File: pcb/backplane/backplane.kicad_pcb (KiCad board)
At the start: 2 copper layers, 12 parts

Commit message: footprints
added footprints
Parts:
- added JST1: B4B-XH-A, backplane:B4B-XH-A, F.Cu at (62.0, -44.0)
- added JST2: B4B-XH-A, backplane:B4B-XH-A, F.Cu at (44.9, -30.9)
- added JST3: B4B-XH-A, backplane:B4B-XH-A, F.Cu at (44.9, -25.0)
- added JST4: B4B-XH-A, backplane:B4B-XH-A, F.Cu at (62.0, -38.1)
- added Motor1Header1: PRPC006SAAN-RC, backplane:PRPC006SAAN-RC, F.Cu at (28.4, -43.9)
- added Motor1Header2: PRPC006SAAN-RC, backplane:PRPC006SAAN-RC, F.Cu at (28.4, -40.7)
- added Motor1Header3: PRPC006SAAN-RC, backplane:PRPC006SAAN-RC, F.Cu at (45.5, -43.9)
- added Motor2Header1: PRPC006SAAN-RC, backplane:PRPC006SAAN-RC, F.Cu at (28.4, -37.4)
- added Motor2Header2: PRPC006SAAN-RC, backplane:PRPC006SAAN-RC, F.Cu at (45.5, -40.7)
- added Motor2Header3: PRPC006SAAN-RC, backplane:PRPC006SAAN-RC, F.Cu at (28.4, -34.1)
- added Motor3Header1: PRPC006SAAN-RC, backplane:PRPC006SAAN-RC, F.Cu at (28.4, -30.8)
- added Motor3Header2: PRPC006SAAN-RC, backplane:PRPC006SAAN-RC, F.Cu at (28.4, -27.5)
- added Motor3Header3: PRPC006SAAN-RC, backplane:PRPC006SAAN-RC, F.Cu at (28.4, -24.2)
- added Motor4Header1: PRPC006SAAN-RC, backplane:PRPC006SAAN-RC, F.Cu at (28.4, -20.9)
- added Motor4Header2: PRPC006SAAN-RC, backplane:PRPC006SAAN-RC, F.Cu at (45.5, -37.4)
- added Motor4Header3: PRPC006SAAN-RC, backplane:PRPC006SAAN-RC, F.Cu at (45.5, -34.1)

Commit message: updated pcb
added footprints and schematic
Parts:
- removed Motor1Header1, Motor1Header2, Motor1Header3, Motor2Header1, Motor2Header2, Motor2Header3, Motor3Header1, Motor3Header2, Motor3Header3, Motor4Header1, Motor4Header2, Motor4Header3: PRPC006SAAN-RC, backplane:PRPC006SAAN-RC
- added JST5: B4B-XH-A, backplane:B4B-XH-A, F.Cu at (5.08, 87.7)
- added JST6: B4B-XH-A, backplane:B4B-XH-A, F.Cu at (5.08, 53.3)
- added JST7: B4B-XH-A, backplane:B4B-XH-A, F.Cu at (121.9, 53.3)
- added JST8: B4B-XH-A, backplane:B4B-XH-A, F.Cu at (121.9, 88.9)
- added U1: 74LVCH2T45DC,125, backplane:74LVCH2T45DC,125, F.Cu at (22.9, 30.5)
- added U2: 74LVCH2T45DC,125, backplane:74LVCH2T45DC,125, F.Cu at (22.9, 68.6)
- added U3: 74LVCH2T45DC,125, backplane:74LVCH2T45DC,125, F.Cu at (108.1, 30.7)
- added U4: 74LVCH2T45DC,125, backplane:74LVCH2T45DC,125, F.Cu at (106.7, 68.6)
- added barrelJack1: PJ-037A, backplane:PJ-037A, F.Cu at (64.8, 6.35)
- added barrelJack2: PJ-037A, backplane:PJ-037A, F.Cu at (77.5, 6.35)
- added barrelJack3: PJ-037A, backplane:PJ-037A, F.Cu at (53.3, 6.35)
- added encoderpins1: PREC002SAAN-RC, backplane:PREC002SAAN-RC, F.Cu at (34.3, 41.9)
- added encoderpins2: PREC002SAAN-RC, backplane:PREC002SAAN-RC, F.Cu at (33.0, 90.2)
- added encoderpins3: PREC002SAAN-RC, backplane:PREC002SAAN-RC, F.Cu at (94.0, 50.8)
- added encoderpins4: PREC002SAAN-RC, backplane:PREC002SAAN-RC, F.Cu at (94.0, 86.4)
- added encoderpins5: PREC002SAAN-RC, backplane:PREC002SAAN-RC, F.Cu at (34.3, 31.8)
- added encoderpins6: PREC002SAAN-RC, backplane:PREC002SAAN-RC, F.Cu at (33.0, 69.8)
- added encoderpins7: PREC002SAAN-RC, backplane:PREC002SAAN-RC, F.Cu at (94.0, 31.8)
- added encoderpins8: PREC002SAAN-RC, backplane:PREC002SAAN-RC, F.Cu at (94.0, 71.1)
- moved JST4 126.8 mm to (121.9, 73.7), turned to 90 degrees
- moved motor2Gnd1 120.1 mm to (119.4, 7.62), turned to 180 degrees
- moved motor3Gnd1 117.0 mm to (7.62, 119.4), turned to 0 degrees
- moved motor3Pwr1 117.0 mm to (7.62, 105.4), turned to 0 degrees
- moved motor2Pwr1 113.7 mm to (119.4, 21.6), turned to 180 degrees
- moved JST3 106.4 mm to (5.08, 73.7), turned to 270 degrees
- moved JST2 103.4 mm to (121.9, 38.1), turned to 90 degrees
- moved JST1 101.0 mm to (5.08, 39.4), turned to 270 degrees
- moved motor4Gnd1 86.7 mm to (119.4, 119.4), turned to 180 degrees
- moved motor4Pwr1 86.7 mm to (119.4, 105.4), turned to 180 degrees
- moved lipo2Gnd1 65.7 mm to (99.1, 119.4), turned to 180 degrees
- moved lipo1Gnd1 54.0 mm to (41.9, 119.4)
- moved lipo1Pwr1 54.0 mm to (27.9, 119.4)
- moved lipo2Pwr1 51.8 mm to (85.1, 119.4)
- moved motor1Pwr1 1.80 mm to (7.62, 7.62), turned to 0 degrees
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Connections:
- JST1 pad 1: Motor1EncoderPin1 -> +5V
- JST1 pad 2: Motor1EncoderPin2 -> GND
- JST1 pad 3: Motor1EncoderPin3 -> Motor1EncoderA
- JST1 pad 4: Motor1EncoderPin4 -> Motor1EncoderB
- JST2 pad 1: Motor2EncoderPin1 -> +5V
- JST2 pad 2: Motor2EncoderPin2 -> GND
- JST2 pad 3: Motor2EncoderPin3 -> Motor2EncoderA
- JST2 pad 4: Motor2EncoderPin4 -> Motor2EncoderB
- JST3 pad 1: Motor3EncoderPin1 -> +5V
- JST3 pad 2: Motor3EncoderPin2 -> GND
- JST3 pad 3: Motor3EncoderPin3 -> Motor3EncoderA
- JST3 pad 4: Motor3EncoderPin4 -> Motor3EncoderB
- JST4 pad 1: Motor4EncoderPin1 -> +5V
- JST4 pad 2: Motor4EncoderPin2 -> GND
- JST4 pad 3: Motor4EncoderPin3 -> Motor4EncoderA
- JST4 pad 4: Motor4EncoderPin4 -> Motor4EncoderB
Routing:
- net Motor2EncoderB: track 0.00 -> 2.62 mm
- net Motor2EncoderA: track 0.00 -> 2.57 mm
- net Motor1EncoderA: track 0.00 -> 2.46 mm
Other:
- board outline added: 127 x 127 mm
- net class Default: trace_width 0.25 -> 0.3; via_dia 0.8 -> 0.762; via_drill 0.4 -> 0.381
- rule pad_to_mask_clearance: 0.051 -> 0.0508
- rule trace_min: 0.2 -> 0.1524
- rule via_min_drill: 0.3 -> 0.254
- rule via_min_size: 0.4 -> 0.508

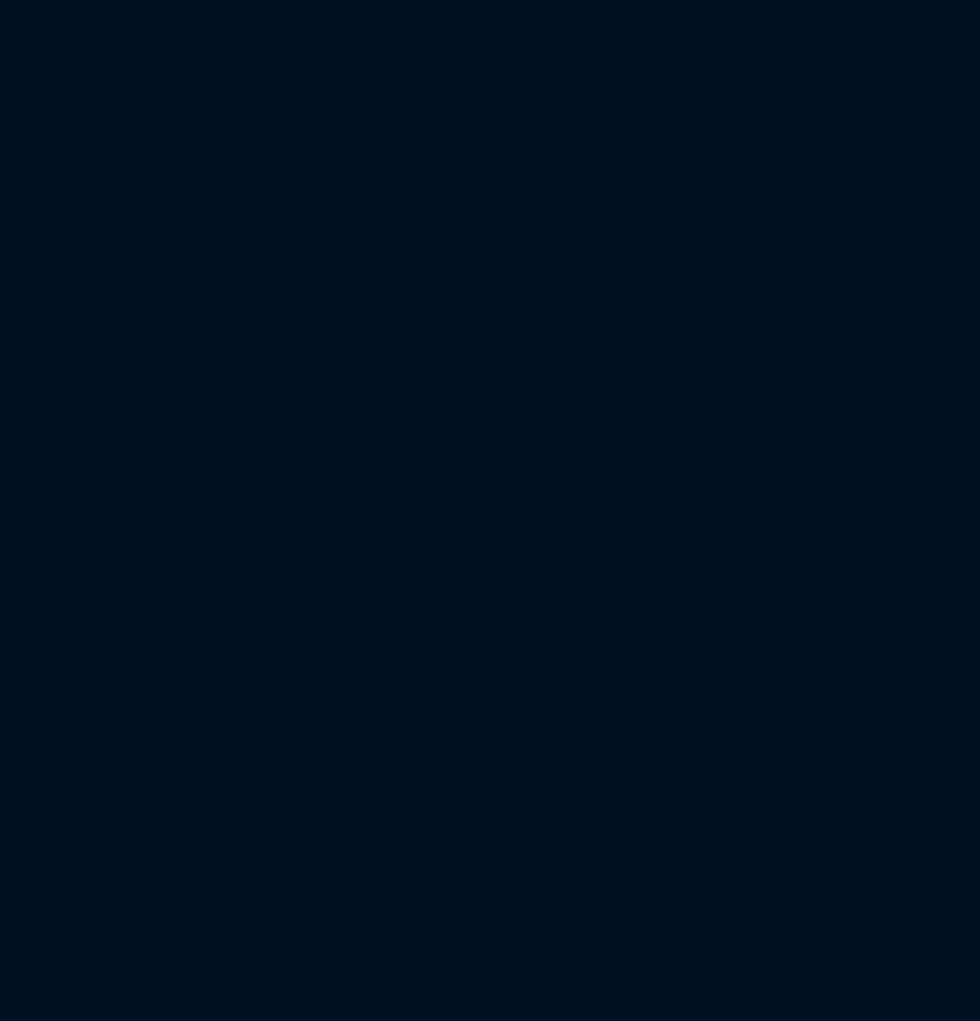
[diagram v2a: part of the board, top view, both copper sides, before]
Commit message: updated footprints
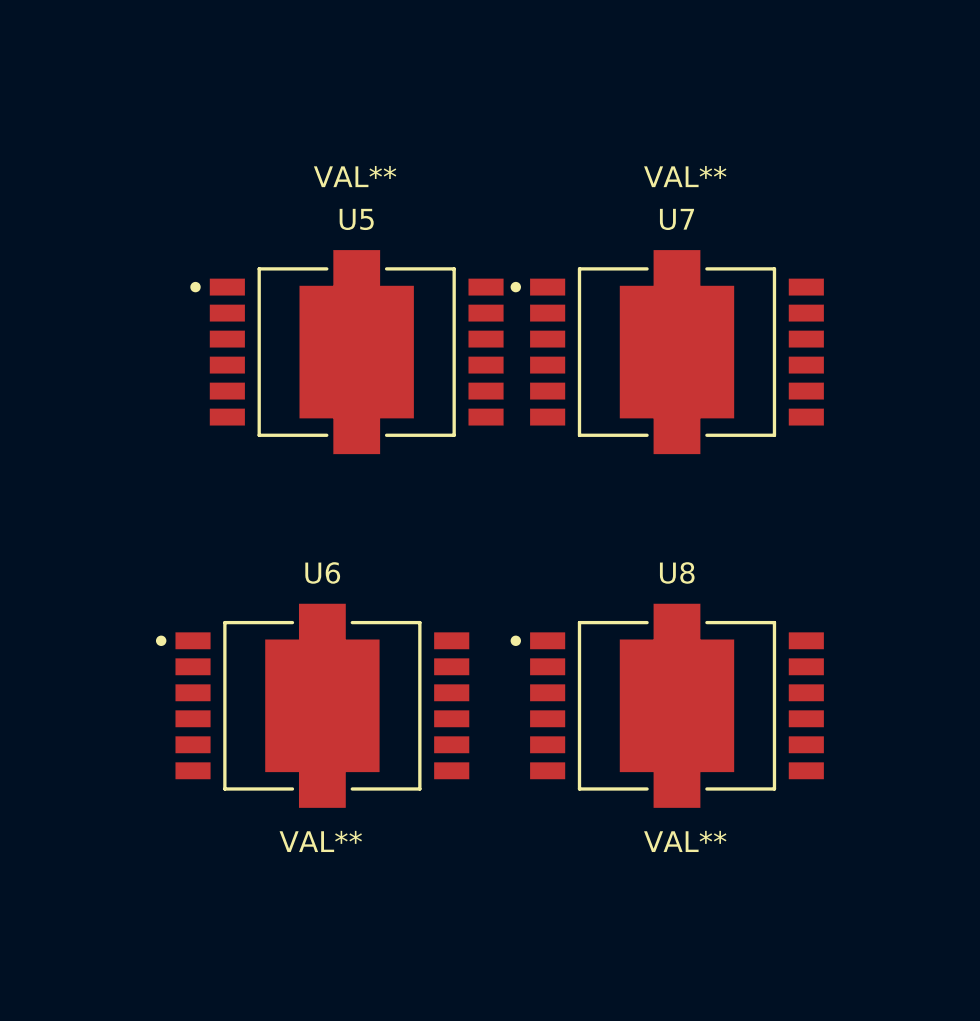
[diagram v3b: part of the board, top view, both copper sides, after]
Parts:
- added U5: VAL**, backplane:IFX9201SGAUMA1, F.Cu at (57.2, 46.1)
- added U6: VAL**, backplane:IFX9201SGAUMA1, F.Cu at (55.9, 59.7)
- added U7: VAL**, backplane:IFX9201SGAUMA1, F.Cu at (69.5, 46.1)
- added U8: VAL**, backplane:IFX9201SGAUMA1, F.Cu at (69.5, 59.7)

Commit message: updates
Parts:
- removed U2, U3, U4: 74LVCH2T45DC,125, backplane:74LVCH2T45DC,125
- removed lipo1Gnd1, lipo1Pwr1, lipo2Gnd1, lipo2Pwr1, motor1Gnd1, motor1Pwr1, motor2Gnd1, motor2Pwr1, motor3Gnd1, motor3Pwr1, motor4Gnd1, motor4Pwr1: CT3151V1-5, backplane:CT3151V1-5
- added LipoGnd1: 1336G1, backplane:1336G1, F.Cu at (54.6, 114.3)
- added levelShift1: 74LVCH2T45DC,125, backplane:74LVCH2T45DC,125, F.Cu at (20.3, 31.8)
- added levelShift2: 74LVCH2T45DC,125, backplane:74LVCH2T45DC,125, F.Cu at (102.9, 43.2)
- added levelShift3: 74LVCH2T45DC,125, backplane:74LVCH2T45DC,125, F.Cu at (16.5, 69.8)
- added levelShift4: 74LVCH2T45DC,125, backplane:74LVCH2T45DC,125, F.Cu at (108.0, 66.0)
- added lipoGnd1: 1336G1, backplane:1336G1, F.Cu at (85.1, 114.3)
- added lipoIn1: 1336G1, backplane:1336G1, F.Cu at (39.4, 114.3)
- added lipoIn2: 1336G1, backplane:1336G1, F.Cu at (69.8, 114.3)
- added motorGnd1: 1336G1, backplane:1336G1, F.Cu at (14.0, 22.9)
- added motorGnd2: 1336G1, backplane:1336G1, F.Cu at (113.0, 22.9)
- added motorGnd3: 1336G1, backplane:1336G1, F.Cu at (15.2, 119.4)
- added motorGnd4: 1336G1, backplane:1336G1, F.Cu at (111.8, 119.4)
- added motorPwm1: 1336G1, backplane:1336G1, F.Cu at (14.0, 7.62)
- added motorPwm2: 1336G1, backplane:1336G1, F.Cu at (113.0, 7.62)
- added motorPwm3: 1336G1, backplane:1336G1, F.Cu at (15.2, 104.1)
- added motorPwm4: 1336G1, backplane:1336G1, F.Cu at (111.8, 104.1)
- added rail12v1: AP6503SP-13, backplane:AP6503SP-13, F.Cu at (76.2, 27.9)
- added rail3v3: AP6503SP-13, backplane:AP6503SP-13, F.Cu at (64.8, 27.9)
- added rail5v1: AP6503SP-13, backplane:AP6503SP-13, F.Cu at (54.6, 27.9)
- U1: value 74LVCH2T45DC,125 -> PCA9685PW; footprint backplane:74LVCH2T45DC,125 -> Package_SO:TSSOP-28_4.4x9.7mm_P0.65mm
- U5, U6, U7, U8: value VAL** -> IFX9201SGAUMA1
- moved U7 71.4 mm to (31.8, 106.7)
- moved U6 63.8 mm to (99.1, 12.7)
- moved U8 56.6 mm to (99.1, 108.0)
- moved U5 41.8 mm to (30.5, 14.0)
- moved U1 33.1 mm to (50.8, 48.3)
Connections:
- U1 pad 1: +5V -> Net-(U1-Pad1)
- U1 pad 2: Motor1EncoderA -> Net-(U1-Pad2)
- U1 pad 3: Motor1EncoderB -> Net-(U1-Pad3)
- U1 pad 4: GND -> Net-(U1-Pad4)
- U1 pad 5: GND -> Net-(U1-Pad5)
- U1 pad 6: Motor1EncoderB_3v3 -> Net-(U1-Pad6)
- U1 pad 7: Motor1EncoderA_3v3 -> Net-(U1-Pad7)
- U1 pad 8: +3V3 -> Net-(U1-Pad8)

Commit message: updates
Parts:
- removed U7, U8: IFX9201SGAUMA1, backplane:IFX9201SGAUMA1
- removed motorPwm1, motorPwm2, motorPwm3, motorPwm4: 1336G1, backplane:1336G1
- added C1: 100uF, backplane:865080445010, F.Cu at (85.1, 95.2)
- added C2: 100uF, backplane:865080445010, F.Cu at (31.8, 16.5)
- added C3: 100uF, backplane:865080445010, F.Cu at (87.6, 16.5)
- added C4: 100uF, backplane:865080445010, F.Cu at (41.9, 101.6)
- added C5: 100nF, backplane:865090640001, F.Cu at (31.2, 22.9)
- added C6: 100nF, backplane:865090640001, F.Cu at (40.6, 109.2)
- added C7: 100nF, backplane:865090640001, F.Cu at (82.5, 102.9)
- added C8: 100nF, backplane:865090640001, F.Cu at (88.9, 24.1)
- added U2: IFX9201SGAUMA1, backplane:IFX9201SGAUMA1, F.Cu at (27.9, 106.7)
- added U3: IFX9201SGAUMA1, backplane:IFX9201SGAUMA1, F.Cu at (101.6, 12.7)
- added U4: IFX9201SGAUMA1, backplane:IFX9201SGAUMA1, F.Cu at (95.2, 104.1)
- added motorControl1: PREC002SAAN-RC, backplane:PREC002SAAN-RC, F.Cu at (66.0, 80.0)
- added motorControl2: PREC002SAAN-RC, backplane:PREC002SAAN-RC, F.Cu at (50.1, 87.6)
- added motorControl3: PREC002SAAN-RC, backplane:PREC002SAAN-RC, F.Cu at (50.1, 80.4)
- added motorControl4: PREC002SAAN-RC, backplane:PREC002SAAN-RC, F.Cu at (64.8, 87.6)
- added motorControlOut1: 1336G1, backplane:1336G1, F.Cu at (14.0, 7.62)
- added motorControlOut2: 1336G1, backplane:1336G1, F.Cu at (113.0, 7.62)
- added motorControlOut3: 1336G1, backplane:1336G1, F.Cu at (15.2, 104.1)
- added motorControlOut4: 1336G1, backplane:1336G1, F.Cu at (111.8, 104.1)
- U5: value IFX9201SGAUMA1 -> PREC004SAAN-RC; footprint backplane:IFX9201SGAUMA1 -> backplane:PREC004SAAN-RC
- moved U6 76.3 mm to (22.9, 8.89)
- moved U5 62.7 mm to (63.5, 67.3)
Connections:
- LipoGnd1 pad 1: (no net) -> GND
- U5 pad 1: Net-(U5-Pad1) -> mcuSO
- U5 pad 2: Net-(U5-Pad2) -> mcuSI
- U5 pad 3: Net-(U5-Pad3) -> CSN
- U5 pad 4: Net-(U5-Pad4) -> SCK
- U6 pad 1: Net-(U6-Pad1) -> motorDir1
- U6 pad 10: Net-(U6-Pad10) -> SCK
- U6 pad 11: Net-(U6-Pad11) -> GND
- U6 pad 12: Net-(U6-Pad12) -> motorPwm1
- U6 pad 13: Net-(U6-Pad13) -> GND
- U6 pad 2: Net-(U6-Pad2) -> +3V3
- U6 pad 3: Net-(U6-Pad3) -> SO1
- U6 pad 4: Net-(U6-Pad4) -> +14v8
- U6 pad 5: Net-(U6-Pad5) -> motorControlOut1
- U6 pad 6: Net-(U6-Pad6) -> GND
- U6 pad 7: Net-(U6-Pad7) -> motorGnd1
- U6 pad 8: Net-(U6-Pad8) -> mcuSI
- U6 pad 9: Net-(U6-Pad9) -> CSN
- lipoGnd1 pad 1: (no net) -> GND
- lipoIn1 pad 1: (no net) -> +14v8
- lipoIn2 pad 1: (no net) -> +14v8
- motorGnd1 pad 1: (no net) -> motorGnd1
- motorGnd2 pad 1: (no net) -> motorGnd2
- motorGnd3 pad 1: (no net) -> motorGnd3
- motorGnd4 pad 1: (no net) -> motorGnd4
- rail12v1 pad 3: (no net) -> Net-(rail12v1-Pad3)
- rail3v3 pad 3: (no net) -> Net-(rail3v3-Pad3)
- rail5v1 pad 3: (no net) -> Net-(rail5v1-Pad3)

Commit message: updates
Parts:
- removed U1: PCA9685PW, Package_SO:TSSOP-28_4.4x9.7mm_P0.65mm
- added C10: 47uF, backplane:865090449007, F.Cu at (71.1, -33.0)
- added C11: 10nF, Capacitor_SMD:C_1206_3216Metric_Pad1.42x1.75mm_HandSolder, F.Cu at (138.4, -41.1)
- added C12: 100nF, Capacitor_SMD:C_1206_3216Metric_Pad1.42x1.75mm_HandSolder, F.Cu at (121.0, -24.9)
- added C13: 6.8nF, Capacitor_SMD:C_1206_3216Metric_Pad1.42x1.75mm_HandSolder, F.Cu at (131.0, -32.5)
- added C14: 22uF, backplane:865090442004, F.Cu at (132.2, -38.7)
- added C15: 22uF, backplane:865090442004, F.Cu at (101.6, -77.5)
- added C16: 47uF, backplane:865090449007, F.Cu at (68.6, -63.5)
- added C17: 47uF, backplane:865090449007, F.Cu at (69.8, -48.3)
- added C18: 10nF, Capacitor_SMD:C_1206_3216Metric_Pad1.42x1.75mm_HandSolder, F.Cu at (126.0, -24.9)
- added C19: 10nF, Capacitor_SMD:C_1206_3216Metric_Pad1.42x1.75mm_HandSolder, F.Cu at (131.0, -30.2)
- added C20: 100nF, Capacitor_SMD:C_1206_3216Metric_Pad1.42x1.75mm_HandSolder, F.Cu at (130.9, -24.9)
- added C21: 6.8nF, Capacitor_SMD:C_1206_3216Metric_Pad1.42x1.75mm_HandSolder, F.Cu at (135.9, -27.9)
- added C22: 100nF, Capacitor_SMD:C_1206_3216Metric_Pad1.42x1.75mm_HandSolder, F.Cu at (140.9, -34.2)
- added C23: 6.8nF, Capacitor_SMD:C_1206_3216Metric_Pad1.42x1.75mm_HandSolder, F.Cu at (140.9, -36.5)
- added C9: 22uF, backplane:865090442004, F.Cu at (100.3, -55.9)
- added L1: 11uH, backplane:P0847SNL, F.Cu at (34.3, -17.8)
- added L2: 11uH, backplane:P0847SNL, F.Cu at (35.6, -73.7)
- added L3: 11uH, backplane:P0847SNL, F.Cu at (35.6, -47.0)
- added R1: 45.3K, Resistor_SMD:R_1206_3216Metric_Pad1.42x1.75mm_HandSolder, F.Cu at (150.5, -45.8)
- added R10: 6.8k, Resistor_SMD:R_1206_3216Metric_Pad1.42x1.75mm_HandSolder, F.Cu at (135.9, -34.8)
- added R11: 100K, Resistor_SMD:R_1206_3216Metric_Pad1.42x1.75mm_HandSolder, F.Cu at (145.6, -45.8)
- added R12: 100K, Resistor_SMD:R_1206_3216Metric_Pad1.42x1.75mm_HandSolder, F.Cu at (145.6, -48.1)
- added R2: 10K, Resistor_SMD:R_1206_3216Metric_Pad1.42x1.75mm_HandSolder, F.Cu at (143.3, -38.8)
- added R3: 6.8k, Resistor_SMD:R_1206_3216Metric_Pad1.42x1.75mm_HandSolder, F.Cu at (135.9, -30.2)
- added R4: 100K, Resistor_SMD:R_1206_3216Metric_Pad1.42x1.75mm_HandSolder, F.Cu at (138.4, -38.8)
- added R5: 120K, Resistor_SMD:R_1206_3216Metric_Pad1.42x1.75mm_HandSolder, F.Cu at (135.9, -32.5)
- added R6: 10K, Resistor_SMD:R_1206_3216Metric_Pad1.42x1.75mm_HandSolder, F.Cu at (143.3, -41.1)
- added R7: 26.1K, Resistor_SMD:R_1206_3216Metric_Pad1.42x1.75mm_HandSolder, F.Cu at (131.0, -27.9)
- added R8: 10K, Resistor_SMD:R_1206_3216Metric_Pad1.42x1.75mm_HandSolder, F.Cu at (150.5, -48.1)
- added R9: 6.8k, Resistor_SMD:R_1206_3216Metric_Pad1.42x1.75mm_HandSolder, F.Cu at (146.8, -43.5)
- C5, C6, C7, C8: footprint backplane:865090640001 -> Capacitor_SMD:C_1206_3216Metric_Pad1.42x1.75mm_HandSolder
- moved C4 171.6 mm to (83.8, -64.8)
- moved C6 170.0 mm to (131.0, -34.8)
- moved C7 157.9 mm to (141.9, -43.4)
- moved C1 129.7 mm to (104.1, -33.0)
- moved C5 124.8 mm to (136.9, -43.4)
- moved C2 110.5 mm to (111.8, -59.7)
- moved C8 95.2 mm to (148.1, -50.4)
- moved C3 62.8 mm to (102.9, -44.5)
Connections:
- rail12v1 pad 2: Net-(rail12v1-Pad2) -> +14v8
- rail12v1 pad 4: Net-(rail12v1-Pad4) -> GND
- rail12v1 pad 9: Net-(rail12v1-Pad9) -> GND
- rail3v3 pad 2: Net-(rail3v3-Pad2) -> +14v8
- rail3v3 pad 4: Net-(rail3v3-Pad4) -> GND
- rail3v3 pad 9: Net-(rail3v3-Pad9) -> GND
- rail5v1 pad 2: Net-(rail5v1-Pad2) -> +14v8
- rail5v1 pad 4: Net-(rail5v1-Pad4) -> GND
- rail5v1 pad 9: Net-(rail5v1-Pad9) -> GND

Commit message: updates
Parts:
- L1, L2, L3: value 11uH -> 15uH; footprint backplane:P0847SNL -> backplane:6100-150K-RC
- moved levelShift1 260.5 mm to (280.7, 24.0)
- moved U2 253.5 mm to (263.3, 12.5)
- moved encoderpins2 252.2 mm to (276.1, 23.0), turned to 0 degrees
- moved encoderpins6 248.1 mm to (276.1, 20.1), turned to 0 degrees
- moved levelShift3 247.6 mm to (262.8, 44.2)
- moved L1 242.6 mm to (274.8, 14.2)
- moved JST6 241.9 mm to (246.0, 32.3), turned to 0 degrees
- moved L3 237.0 mm to (257.9, 34.9)
- moved motorGnd1 235.5 mm to (249.4, 28.2), turned to 0 degrees
- moved JST5 234.9 mm to (233.4, 32.3), turned to 0 degrees
- moved L2 234.2 mm to (232.6, 52.9)
- moved rail5v1 229.4 mm to (283.4, 11.8)
- moved motorControl3 228.8 mm to (270.8, 20.1)
- moved motorControl2 224.0 mm to (266.2, 28.5)
- moved rail3v3 219.9 mm to (283.4, 3.93)
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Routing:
- net Motor2EncoderB: track 2.62 -> 0.00 mm
- net Motor2EncoderA: track 2.57 -> 0.00 mm
- net Motor1EncoderA: track 2.46 -> 0.00 mm
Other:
- board size 127 x 127 mm -> 101.6 x 101.6 mm
